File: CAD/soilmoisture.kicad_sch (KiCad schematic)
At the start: 11 parts, among them J1 Conn_ARM_JTAG_SWD_10, J2 Conn_01x02 0.1", U1 BT840, U2 BAT-HLD-001, Y1 ABS07-32.768KHZ-T

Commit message: blinktest
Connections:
- net GND: now also U1.P$A0 (A0/VSS1), U1.P$B0 (B0/VSS2), U1.P$C0 (C0/VSS3), U1.P$D0 (D0/VSS4)
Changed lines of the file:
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@@
+    )
+  )
+  (symbol (lib_id "power:GND") (at 151.13 101.6 0) (unit 1)
+    (in_bom yes) (on_board yes) (dnp no)
+    (property "Reference" "#PWR019" (at 151.13 107.95 0)
+      (effects (font (size 1.27 1.27)) hide)
+    )
+    (property "Value" "GND" (at 151.257 105.9942 0)
+      (effects (font (size 1.27 1.27)))
+    )
+    (property "Footprint" "" (at 151.13 101.6 0)
+      (effects (font (size 1.27 1.27)) hide)
+    )
+    (property "Datasheet" "" (at 151.13 101.6 0)
+      (effects (font (size 1.27 1.27)) hide)
+    )
+    (pin "1")
+    (instances
+      (project "soilmoisture"
+        (path "/0d83ea7b-58b2-465b-bd1b-b8fa23c41812"
+          (reference "#PWR019") (unit 1)
+        )
+      )
     )
   )
@@
         (path "/0d83ea7b-58b2-465b-bd1b-b8fa23c41812"
           (reference "#PWR017") (unit 1)
+        )
+      )
+    )
+  )
+  (symbol (lib_id "power:GND") (at 133.35 101.6 0) (unit 1)
+    (in_bom yes) (on_board yes) (dnp no)
+    (property "Reference" "#PWR018" (at 133.35 107.95 0)
+      (effects (font (size 1.27 1.27)) hide)
+    )
+    (property "Value" "GND" (at 133.477 105.9942 0)
+      (effects (font (size 1.27 1.27)))
+    )
+    (property "Footprint" "" (at 133.35 101.6 0)
+      (effects (font (size 1.27 1.27)) hide)
+    )
+    (property "Datasheet" "" (at 133.35 101.6 0)
+      (effects (font (size 1.27 1.27)) hide)
+    )
+    (pin "1")
+    (instances
+      (project "soilmoisture"
+        (path "/0d83ea7b-58b2-465b-bd1b-b8fa23c41812"
+          (reference "#PWR018") (unit 1)
         )
       )
@@
     )
   )
+  (symbol (lib_id "power:GND") (at 115.57 101.6 0) (unit 1)
+    (in_bom yes) (on_board yes) (dnp no)
+    (property "Reference" "#PWR012" (at 115.57 107.95 0)
+      (effects (font (size 1.27 1.27)) hide)
+    )
+    (property "Value" "GND" (at 115.697 105.9942 0)
+      (effects (font (size 1.27 1.27)))
+    )
+    (property "Footprint" "" (at 115.57 101.6 0)
+      (effects (font (size 1.27 1.27)) hide)
+    )
+    (property "Datasheet" "" (at 115.57 101.6 0)
+      (effects (font (size 1.27 1.27)) hide)
+    )
+    (pin "1")
+    (instances
+      (project "soilmoisture"
+        (path "/0d83ea7b-58b2-465b-bd1b-b8fa23c41812"
+          (reference "#PWR012") (unit 1)
+        )
+      )
+    )
+  )
   (symbol (lib_id "Device:C") (at 35.56 55.245 90) (unit 1)
     (in_bom yes) (on_board yes) (dnp no) (fields_autoplaced)
@@
         )
       )
+    )
+  )
+  (symbol (lib_id "power:GND") (at 97.79 101.6 0) (unit 1)
+    (in_bom yes) (on_board yes) (dnp no)
+    (property "Reference" "#PWR09" (at 97.79 107.95 0)
+      (effects (font (size 1.27 1.27)) hide)
+    )
+    (property "Value" "GND" (at 97.917 105.9942 0)
+      (effects (font (size 1.27 1.27)))
+    )
+    (property "Footprint" "" (at 97.79 101.6 0)
+      (effects (font (size 1.27 1.27)) hide)
+    )
+    (property "Datasheet" "" (at 97.79 101.6 0)
+      (effects (font (size 1.27 1.27)) hide)
+    )
+    (pin "1")
+    (instances
+      (project "soilmoisture"
+        (path "/0d83ea7b-58b2-465b-bd1b-b8fa23c41812"
+          (reference "#PWR09") (unit 1)
+        )
+      )

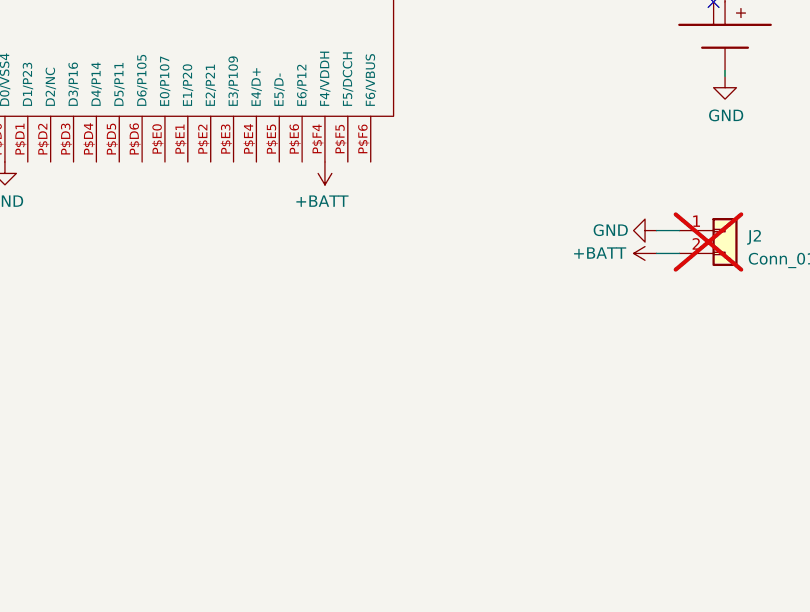
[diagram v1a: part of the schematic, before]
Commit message: Feat: Added inductor
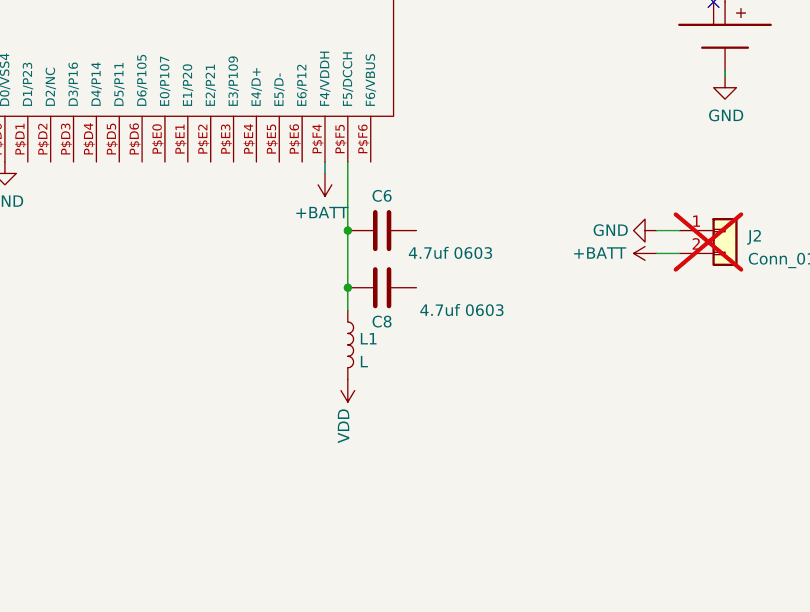
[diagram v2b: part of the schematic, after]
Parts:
- added C6, C8: 4.7uf 0603, Capacitor_SMD:C_0603_1608Metric, symbol Device:C
- added L1: L, symbol Device:L
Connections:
- net VDD: now also L1.2
- net at U1.P$F5 (F5/DCCH): now also C6.1, C8.1, L1.1
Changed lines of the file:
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@@
   (junction (at 41.91 70.485) (diameter 0) (color 0 0 0 0)
   )
+  (junction (at 189.23 115.57) (diameter 0) (color 0 0 0 0)
+  )
   (junction (at 70.485 33.02) (diameter 0) (color 0 0 0 0)
   )
@@
   )
   (junction (at 70.485 36.83) (diameter 0) (color 0 0 0 0)
+  )
+  (junction (at 189.23 109.22) (diameter 0) (color 0 0 0 0)
   )
   (junction (at 70.485 40.64) (diameter 0) (color 0 0 0 0)
@@
     (stroke (width 0) (type default))
   )
+  (wire (pts (xy 189.23 115.57) (xy 189.23 109.22))
+    (stroke (width 0) (type default))
+  )
   (wire (pts (xy 50.8 66.04) (xy 72.39 66.04))
     (stroke (width 0) (type default))
@@
     (stroke (width 0) (type default))
   )
+  (wire (pts (xy 186.69 101.6) (xy 186.69 102.87))
+    (stroke (width 0) (type default))
+  )
   (wire (pts (xy 72.39 29.21) (xy 70.485 29.21))
     (stroke (width 0) (type default))
@@
     (stroke (width 0) (type default))
   )
+  (wire (pts (xy 189.23 109.22) (xy 189.23 101.6))
+    (stroke (width 0) (type default))
+  )
   (wire (pts (xy 70.485 29.21) (xy 70.485 33.02))
     (stroke (width 0) (type default))
@@
   )
   (wire (pts (xy 199.39 54.61) (xy 200.025 54.61))
+    (stroke (width 0) (type default))
+  )
+  (wire (pts (xy 189.23 118.11) (xy 189.23 115.57))
     (stroke (width 0) (type default))
   )
@@
     )
   )
-  (symbol (lib_id "power:+BATT") (at 186.69 101.6 180) (unit 1)
-    (in_bom yes) (on_board yes) (dnp no)
-    (property "Reference" "#PWR0104" (at 186.69 97.79 0)
-      (effects (font (size 1.27 1.27)) hide)
-    )
-    (property "Value" "+BATT" (at 186.309 105.9942 0)
-      (effects (font (size 1.27 1.27)))
-    )
-    (property "Footprint" "" (at 186.69 101.6 0)
-      (effects (font (size 1.27 1.27)) hide)
-    )
-    (property "Datasheet" "" (at 186.69 101.6 0)
+  (symbol (lib_id "power:+BATT") (at 186.69 102.87 180) (unit 1)
+    (in_bom yes) (on_board yes) (dnp no)
+    (property "Reference" "#PWR0104" (at 186.69 99.06 0)
+      (effects (font (size 1.27 1.27)) hide)
+    )
+    (property "Value" "+BATT" (at 186.309 107.2642 0)
+      (effects (font (size 1.27 1.27)))
+    )
+    (property "Footprint" "" (at 186.69 102.87 0)
+      (effects (font (size 1.27 1.27)) hide)
+    )
+    (property "Datasheet" "" (at 186.69 102.87 0)
       (effects (font (size 1.27 1.27)) hide)
     )
@@
     )
   )
+  (symbol (lib_id "Device:L") (at 189.23 121.92 0) (unit 1)
+    (in_bom yes) (on_board yes) (dnp no) (fields_autoplaced)
+    (property "Reference" "L1" (at 190.5 121.285 0)
+      (effects (font (size 1.27 1.27)) (justify left))
+    )
+    (property "Value" "L" (at 190.5 123.825 0)
+      (effects (font (size 1.27 1.27)) (justify left))
+    )
+    (property "Footprint" "" (at 189.23 121.92 0)
+      (effects (font (size 1.27 1.27)) hide)
+    )
+    (property "Datasheet" "~" (at 189.23 121.92 0)
+      (effects (font (size 1.27 1.27)) hide)
+    )
+    (pin "1")
+    (pin "2")
+    (instances
+      (project "soilmoisture"
+        (path "/0d83ea7b-58b2-465b-bd1b-b8fa23c41812"
+          (reference "L1") (unit 1)
+        )
+      )
+    )
+  )
   (symbol (lib_id "power:+BATT") (at 223.52 111.76 90) (unit 1)
     (in_bom yes) (on_board yes) (dnp no)
@@
         )
       )
+    )
+  )
+  (symbol (lib_id "power:VDD") (at 189.23 125.73 180) (unit 1)
+    (in_bom yes) (on_board yes) (dnp no)
+    (property "Reference" "#PWR020" (at 189.23 121.92 0)
+      (effects (font (size 1.27 1.27)) hide)
+    )
+    (property "Value" "VDD" (at 188.7982 128.9812 90)
+      (effects (font (size 1.27 1.27)) (justify left))
+    )
+    (property "Footprint" "" (at 189.23 125.73 0)
+      (effects (font (size 1.27 1.27)) hide)
+    )
+    (property "Datasheet" "" (at 189.23 125.73 0)
+      (effects (font (size 1.27 1.27)) hide)
+    )
+    (pin "1")
+    (instances
+      (project "soilmoisture"
+        (path "/0d83ea7b-58b2-465b-bd1b-b8fa23c41812"
+          (reference "#PWR020") (unit 1)
+        )
+      )
+    )
+  )
+  (symbol (lib_id "Device:C") (at 193.04 115.57 90) (unit 1)
+    (in_bom yes) (on_board yes) (dnp no)
+    (property "Reference" "C8" (at 193.04 119.38 90)
+      (effects (font (size 1.27 1.27)))
+    )
+    (property "Value" "4.7uf 0603" (at 201.93 118.11 90)
+      (effects (font (size 1.27 1.27)))
+    )
+    (property "Footprint" "Capacitor_SMD:C_0603_1608Metric" (at 196.85 114.6048 0)
+      (effects (font (size 1.27 1.27)) hide)
+    )
+    (property "Datasheet" "~" (at 193.04 115.57 0)
+      (effects (font (size 1.27 1.27)) hide)
+    )
+    (property "MPN" "CL10A475KQ8NNNC" (at 193.04 115.57 0)
+      (effects (font (size 1.27 1.27)) hide)
+    )
+    (pin "1")
+    (pin "2")
+    (instances
+      (project "soilmoisture"
+        (path "/0d83ea7b-58b2-465b-bd1b-b8fa23c41812"
+          (reference "C8") (unit 1)
+        )
+      )
+    )
+  )
+  (symbol (lib_id "Device:C") (at 193.04 109.22 90) (unit 1)
+    (in_bom yes) (on_board yes) (dnp no)
+    (property "Reference" "C6" (at 193.04 105.41 90)
+      (effects (font (size 1.27 1.27)))
+    )
+    (property "Value" "4.7uf 0603" (at 200.66 111.76 90)
+      (effects (font (size 1.27 1.27)))
+    )
+    (property "Footprint" "Capacitor_SMD:C_0603_1608Metric" (at 196.85 108.2548 0)
+      (effects (font (size 1.27 1.27)) hide)
+    )
+    (property "Datasheet" "~" (at 193.04 109.22 0)
+      (effects (font (size 1.27 1.27)) hide)
+    )
+    (property "MPN" "CL10A475KQ8NNNC" (at 193.04 109.22 0)
+      (effects (font (size 1.27 1.27)) hide)
+    )
+    (pin "1")
+    (pin "2")
+    (instances
+      (project "soilmoisture"
+        (path "/0d83ea7b-58b2-465b-bd1b-b8fa23c41812"
+          (reference "C6") (unit 1)
+        )
+      )
